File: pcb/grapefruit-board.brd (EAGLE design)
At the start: 100 x 50 mm, 151 parts, among them IC1 L70, IC10 TS520525, IC2 STC3100, IC3 TPS61200, IC4 LM3671MF, IC5 MCP73837MF, IC6 LM2840/1/2, IC7 STM32F411XC, IC8 S25FL064K, IC9 TLV320AIC3100, M1 ELECTRET_MICROPHON-WM-62PC/62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, Q1 BSS84, Q2 BSS84, Q3 BSS84, Q4 BSS84, X1 BU-SMA-V, X2 BU-SMA-V, X3 BU-SMA-V, X4 USB-MICROB, X5 USB-MICROB, Y1 32768Hz

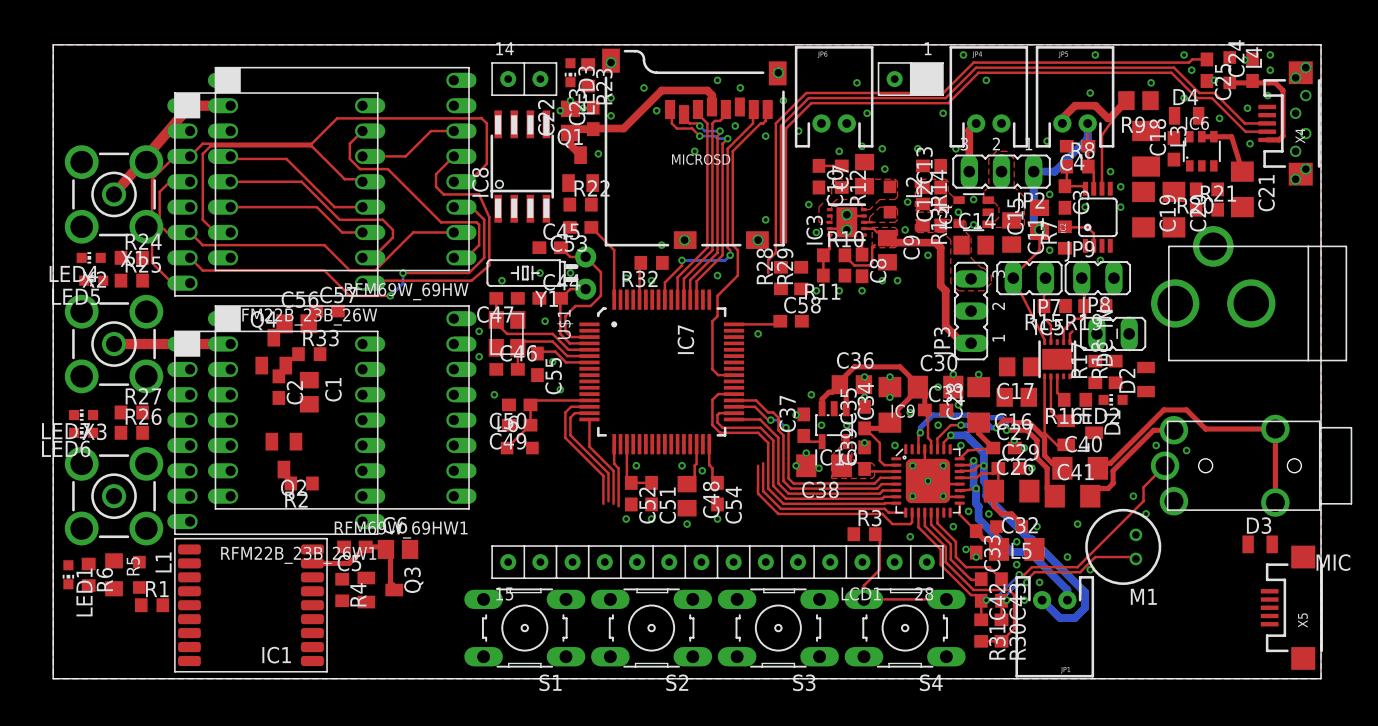
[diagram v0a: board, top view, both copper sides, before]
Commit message: Change values of some components, add SWD pin header
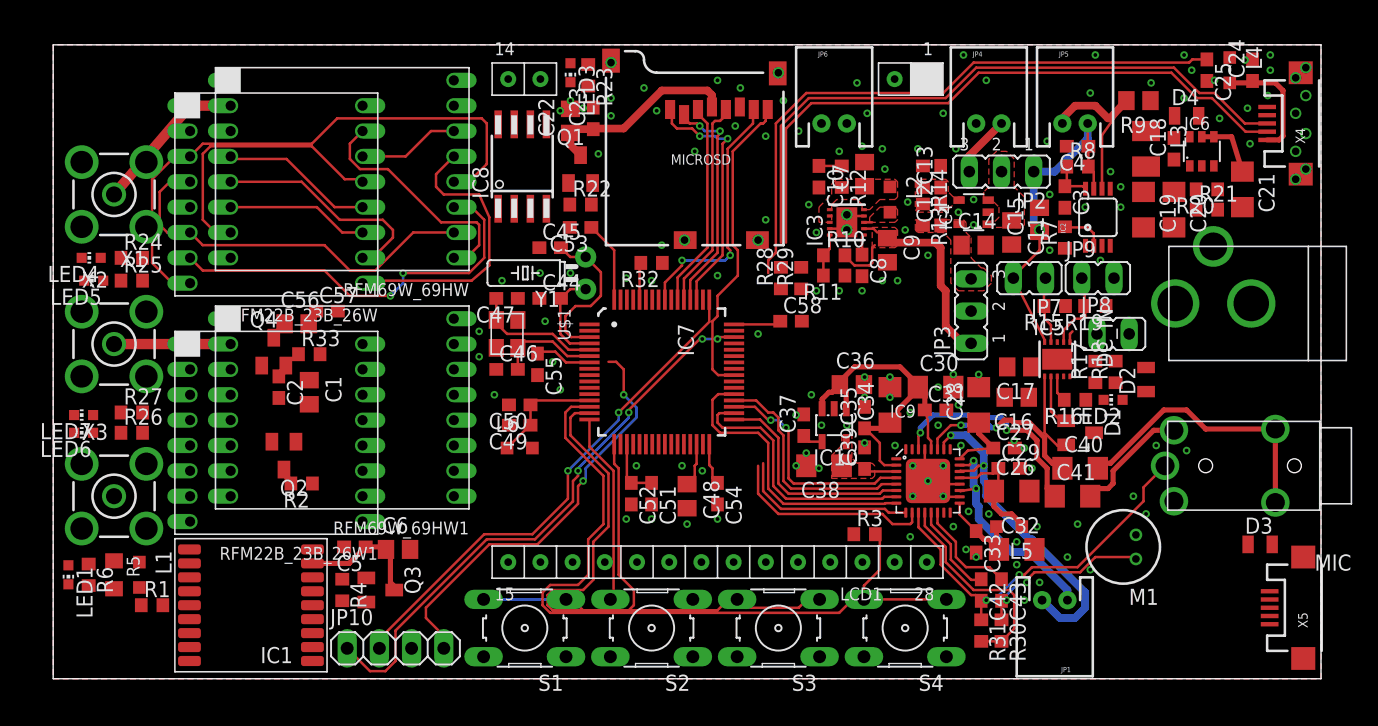
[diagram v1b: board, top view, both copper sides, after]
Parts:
- added JP10: (no value), pinhead:1X04
- C46, C47: value 12pF -> 22pF
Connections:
- removed net N$53: C55.1, IC7.7
- new net NRST: C55.1, IC7.7, JP10.4
- new net SWCLK: IC7.49, JP10.2
- new net SWDIO: IC7.46, JP10.1
- new net USART1_RX: IC7.55
- new net USART1_TX: IC7.50
- net GND: now also JP10.3, JP4.1; no longer JP4.2
- net N$10: now also JP4.2; no longer JP4.1
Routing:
- net SWDIO: track 0.00 -> 45.2 mm, vias 0 -> 4
- net SWCLK: track 0.00 -> 40.5 mm, vias 0 -> 2
- net NRST: track 0.00 -> 38.1 mm, vias 0 -> 2
- net BTN4: track 22.8 -> 60.1 mm
- net BTN3: track 9.49 -> 43.6 mm
- net BTN1: track 5.04 -> 25.7 mm
- net BTN2: track 7.44 -> 15.1 mm
- net N$53: track 4.51 -> 0.00 mm
- net N$10: track 4.02 -> 4.85 mm

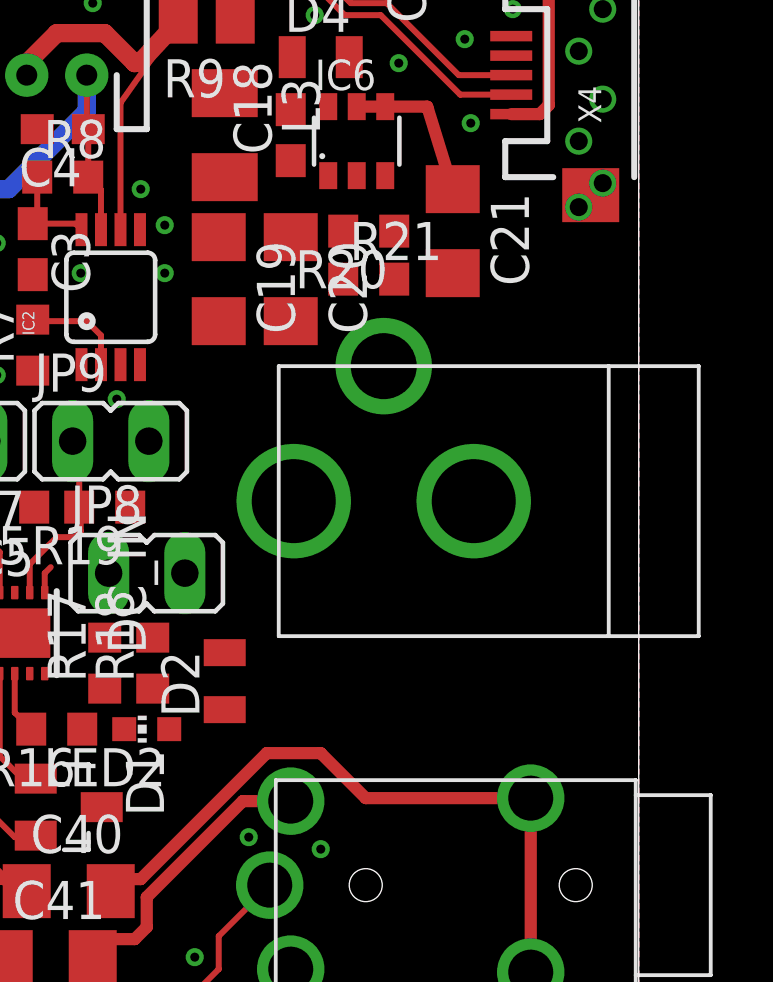
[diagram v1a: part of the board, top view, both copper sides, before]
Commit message: Add DC IN input
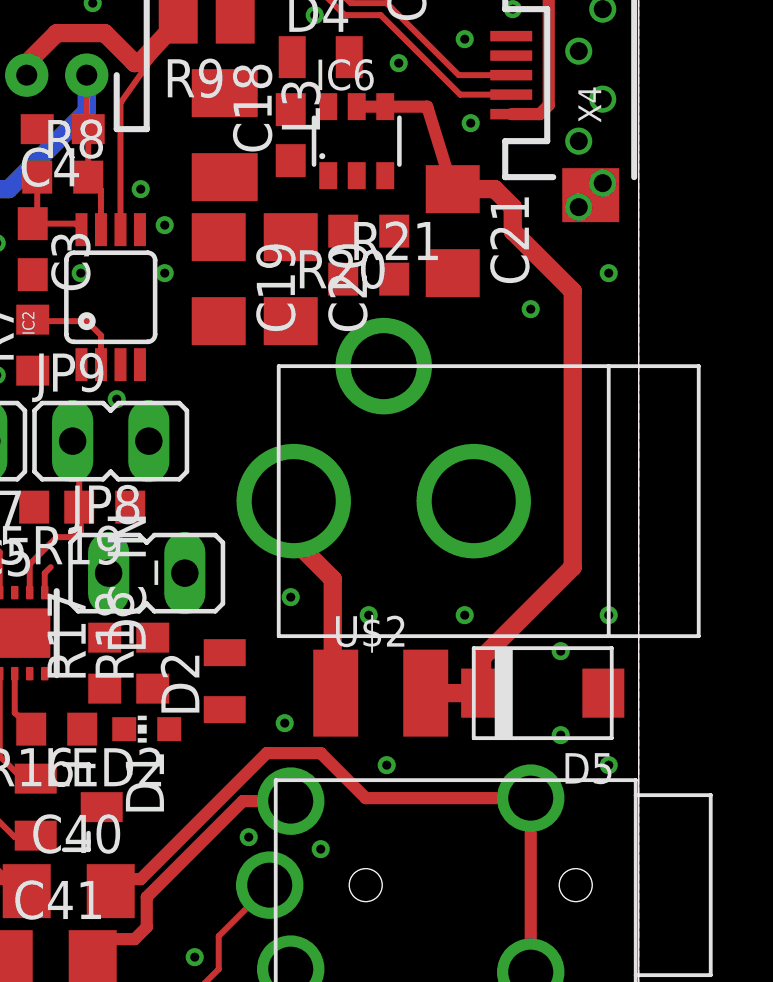
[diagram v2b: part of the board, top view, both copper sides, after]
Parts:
- added D5: 40V, qyx-misc:SMA_DIODE
- added U$2: PTC_FUSE1210, qyx-misc:PTC1210
- DC_IN: value DC_JACK -> 5-40V
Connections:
- new net N$53: DC_IN.C, U$2.1
- net DC_IN: now also D5.K, U$2.2
- net GND: now also D5.A, DC_IN.O, DC_IN.OSW
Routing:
- net DC_IN: track 5.23 -> 27.6 mm
- net N$53: track 0.00 -> 6.98 mm
- net GND: vias 143 -> 154
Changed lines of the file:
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@@
 <element name="MICROSD" library="SparkFun" package="MICRO-SD-SOCKET-PP" value="USD-SOCKETNEW" x="57.6" y="34.2"/>
 <element name="MIC" library="qyx-misc" package="JACK_35_4POLE" value="MJ-2135" x="102.4" y="16.8" rot="R180"/>
-<element name="DC_IN" library="con-qyx" package="DC_JACK" value="DC_JACK" x="95" y="29.6" rot="R90"/>
+<element name="DC_IN" library="con-qyx" package="DC_JACK" value="5-40V" x="95" y="29.6" rot="R90"/>
 <element name="M1" library="microphon" package="WM-62PC/62PK" value="ELECTRET_MICROPHON-WM-62PC/62PK" x="84.4" y="10.4" rot="R180">
 <attribute name="PN" value="PMOF-6027PN-42UQ" x="84.4" y="10.4" size="1.778" layer="27" rot="R180" display="off"/>
@@
 <element name="C58" library="rcl" package="C0603" value="100nF" x="58.2" y="28.2"/>
 <element name="JP10" library="pinhead" package="1X04" value="" x="27" y="2.4"/>
+<element name="U$2" library="qyx-misc" package="PTC1210" value="PTC_FUSE1210" x="91.4" y="23.2"/>
+<element name="D5" library="qyx-misc" package="SMA_DIODE" value="40V" x="96.8" y="23.2" rot="R180"/>
 </elements>
 <signals>
@@
 <contactref element="JP4" pad="1"/>
 <contactref element="JP10" pad="3"/>
+<contactref element="DC_IN" pad="O"/>
+<contactref element="DC_IN" pad="OSW"/>
+<contactref element="D5" pad="A"/>
+<via x="99" y="37.2" extent="1-16" drill="0.3"/>
+<via x="99" y="25.8" extent="1-16" drill="0.3"/>
+<via x="99" y="20.8" extent="1-16" drill="0.3"/>
+<via x="97.4" y="21.8" extent="1-16" drill="0.3"/>
+<via x="97.4" y="24.6" extent="1-16" drill="0.3"/>
+<via x="94.2" y="25.8" extent="1-16" drill="0.3"/>
+<via x="91" y="25.8" extent="1-16" drill="0.3"/>
+<via x="88.4" y="26.4" extent="1-16" drill="0.3"/>
+<via x="88.2" y="22.2" extent="1-16" drill="0.3"/>
+<via x="91.6" y="20.8" extent="1-16" drill="0.3"/>
+<via x="96.4" y="36" extent="1-16" drill="0.3"/>
 </signal>
 <signal name="N$3">
@@
 <wire x1="91.55" y1="42.75" x2="92.95" y2="42.75" width="0.4064" layer="1"/>
 <wire x1="92.95" y1="42.75" x2="93.8" y2="40" width="0.4064" layer="1"/>
+<contactref element="U$2" pad="2"/>
+<contactref element="D5" pad="K"/>
+<wire x1="92.9" y1="23.2" x2="94.78" y2="23.2" width="0.6096" layer="1"/>
+<wire x1="94.78" y1="23.2" x2="94.78" y2="24.38" width="0.6096" layer="1"/>
+<wire x1="94.78" y1="24.38" x2="97.8" y2="27.4" width="0.6096" layer="1"/>
+<wire x1="97.8" y1="27.4" x2="97.8" y2="36.6" width="0.6096" layer="1"/>
+<wire x1="97.8" y1="36.6" x2="95.8" y2="38.6" width="0.6096" layer="1"/>
+<wire x1="95.8" y1="38.6" x2="95.8" y2="39.4" width="0.6096" layer="1"/>
+<wire x1="95.8" y1="39.4" x2="95.2" y2="40" width="0.6096" layer="1"/>
+<wire x1="95.2" y1="40" x2="93.8" y2="40" width="0.6096" layer="1"/>
 </signal>
 <signal name="SDIO_D2">
@@
 <wire x1="25.73" y1="2.4" x2="25.73" y2="3.13" width="0.2" layer="1"/>
 </signal>
+<signal name="N$53">
+<contactref element="DC_IN" pad="C"/>
+<contactref element="U$2" pad="1"/>
+<wire x1="88.5" y1="29.6" x2="88.5" y2="28.3" width="0.6096" layer="1"/>
+<wire x1="88.5" y1="28.3" x2="89.8" y2="27" width="0.6096" layer="1"/>
+<wire x1="89.8" y1="27" x2="89.8" y2="23.3" width="0.6096" layer="1"/>
+<wire x1="89.8" y1="23.3" x2="89.9" y2="23.2" width="0.6096" layer="1"/>
+</signal>
 </signals>

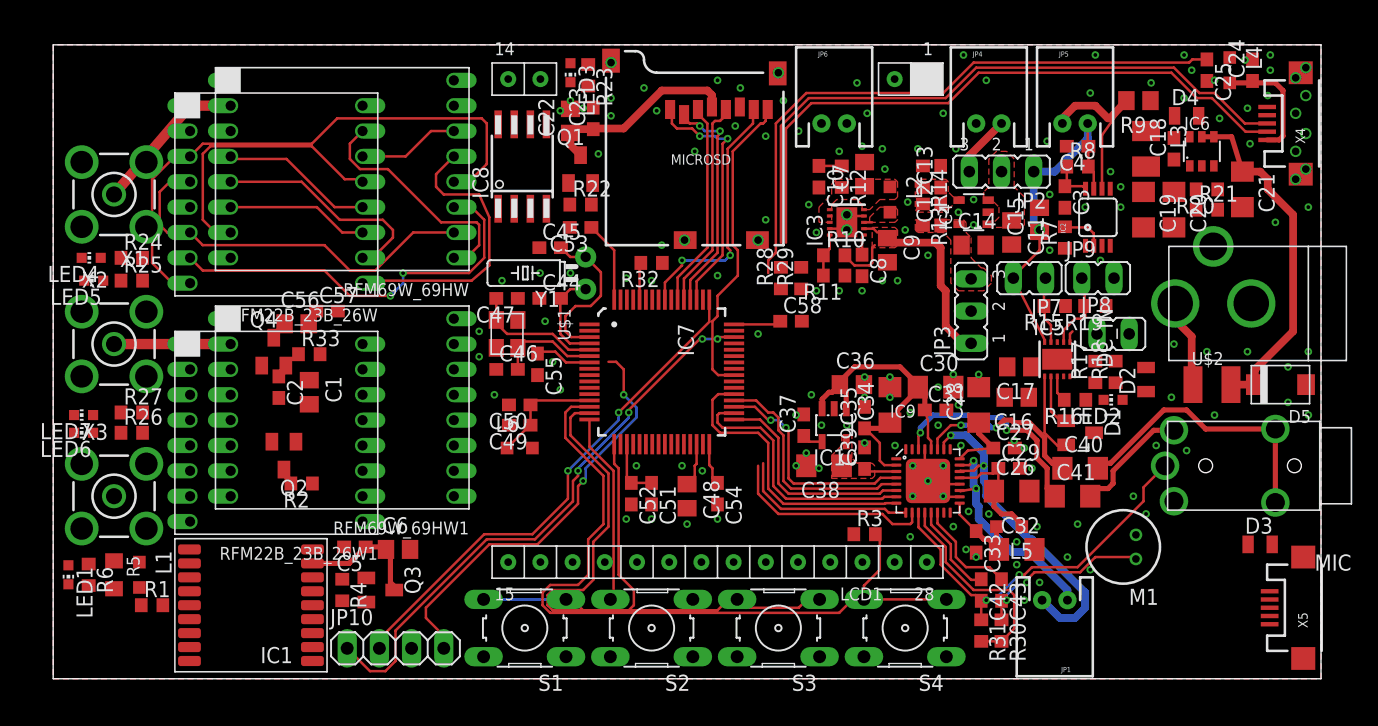
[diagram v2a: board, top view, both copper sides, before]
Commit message: Resolve the remaining unconnected parts
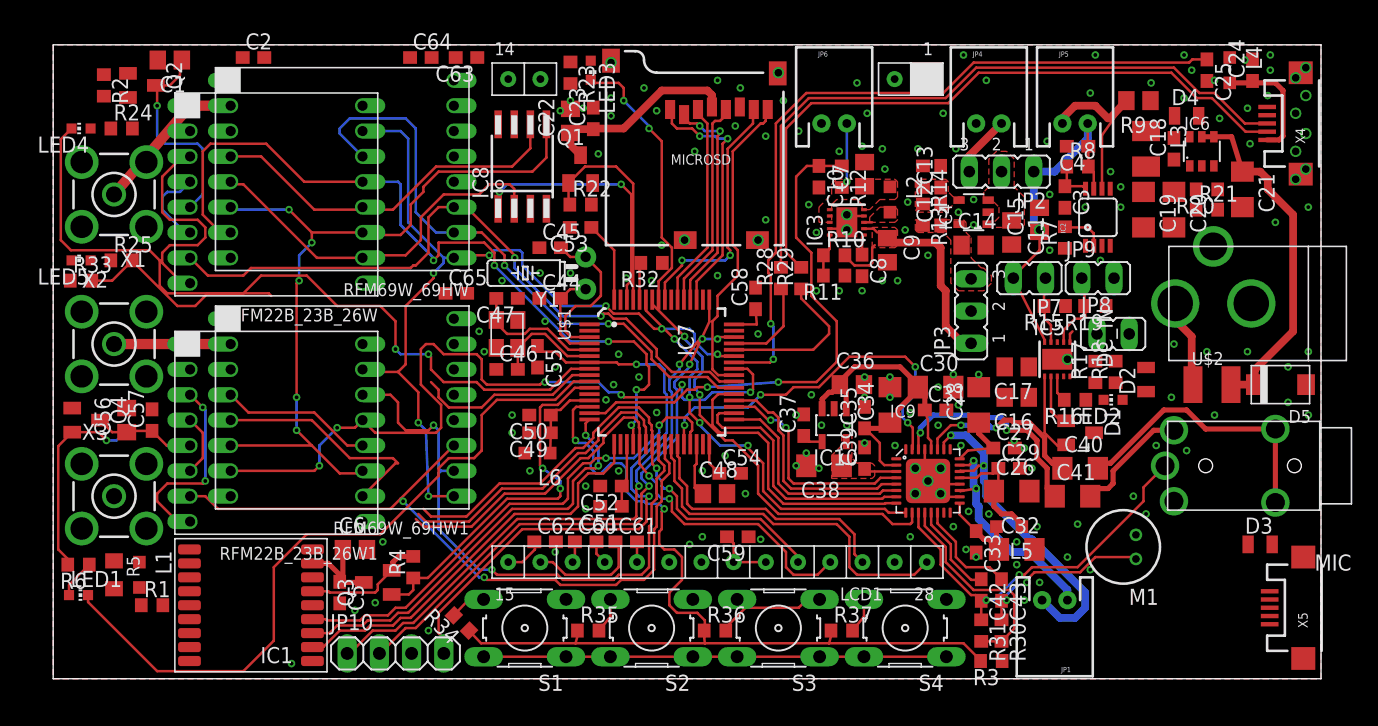
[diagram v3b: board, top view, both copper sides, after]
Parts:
- removed LED6, LED7: (no value), led:CHIP-LED0603
- removed R26, R27: 1K, rcl:R0603
- added C59, C63, C64, C65: 100nF, rcl:C0603
- added C60, C61, C62: 1uF, rcl:C0603
- added R34: 100K, rcl:R0603
- added R35: 47K, rcl:R0603
- added R36: 27K, rcl:R0603
- added R37: 10K, rcl:R0603
- R5: value VARISTORCN0805 -> (none)
- moved R2 35.1 mm to (4.00, 46.8), turned to 270 degrees
- moved Q2 31.3 mm to (7.00, 46.8), turned to 270 degrees
- moved C1 28.4 mm to (9.20, 48.8), turned to 180 degrees
- moved C2 26.1 mm to (15.8, 49.0), turned to 0 degrees
- moved R33 18.9 mm to (2.20, 31.4)
- moved C57 16.3 mm to (7.80, 20.4), turned to 90 degrees
- moved Q4 15.8 mm to (2.60, 20.4), turned to 270 degrees
- moved C56 15.4 mm to (5.80, 20.4), turned to 90 degrees
- moved R3 14.1 mm to (74.0, 1.40), turned to 180 degrees
- moved LED4 10.2 mm to (2.20, 43.4)
- moved R24 10.2 mm to (5.40, 43.4)
- moved R4 5.88 mm to (28.4, 8.80), turned to 90 degrees
- moved C5 3.79 mm to (22.6, 6.80), turned to 270 degrees
- moved C6 3.40 mm to (23.8, 10.2)
- moved C51 3.35 mm to (44.0, 13.6), turned to 180 degrees
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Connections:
- removed net CHG_FULL: IC5.4
- removed net CHG_PG: IC5.8
- removed net CODEC_RESET: IC9.31
- removed net N$33: LED6.A, R26.1
- removed net N$34: LED7.A, R27.1
- removed net R12_MISO: RFM22B_23B_26W.10, RFM22B_23B_26W1.10, RFM69W_69HW.5, RFM69W_69HW1.5
- removed net R12_MOSI: RFM22B_23B_26W.11, RFM22B_23B_26W1.11, RFM69W_69HW.6, RFM69W_69HW1.6
- removed net R12_SCK: RFM22B_23B_26W.12, RFM22B_23B_26W1.12, RFM69W_69HW.4, RFM69W_69HW1.4
- removed net R1_DIO1: RFM22B_23B_26W.7, RFM69W_69HW.11
- removed net R1_DIO3: RFM22B_23B_26W.9, RFM69W_69HW.13
- removed net R1_DIO4: RFM22B_23B_26W.14, RFM69W_69HW.14
- removed net R1_DIO5: RFM69W_69HW.15
- removed net R1_LED1: LED4.C
- removed net R1_LED2: LED5.C
- removed net R1_NSS: RFM22B_23B_26W.13, RFM69W_69HW.7
- removed net R1_RESET: RFM22B_23B_26W.15, RFM69W_69HW.9
- removed net R2_DIO1: RFM22B_23B_26W1.7, RFM69W_69HW1.11
- removed net R2_DIO3: RFM22B_23B_26W1.9, RFM69W_69HW1.13
- removed net R2_DIO4: RFM22B_23B_26W1.14, RFM69W_69HW1.14
- removed net R2_DIO5: RFM69W_69HW1.15
- removed net R2_LED1: LED6.C
- removed net R2_LED2: LED7.C
- removed net R2_NSS: RFM22B_23B_26W1.13, RFM69W_69HW1.7
- removed net R2_RESET: RFM22B_23B_26W1.15, RFM69W_69HW1.9
- removed net VCC: IC8.8
- new net BTN: IC7.14, R3.2, R34.1, R35.1, R36.1, R37.1
- new net CODEC_RST: IC7.28, IC9.31
- new net FLASH1_CS: IC7.62, IC8.1
- new net LCD_CD: IC7.27, LCD1.26
- new net LCD_CS: IC7.26, LCD1.28
- new net N$60: C60.1, LCD1.17
- new net N$61: C61.1, LCD1.16
- new net N$62: C60.2, LCD1.18
- new net N$63: C61.2, LCD1.19
- new net N$64: C62.1, LCD1.15
- new net R12_RESET: IC7.43, RFM22B_23B_26W.15, RFM22B_23B_26W1.15, RFM69W_69HW.9, RFM69W_69HW1.9
- new net R1_CS: IC7.20, RFM22B_23B_26W.13, RFM69W_69HW.7
- new net R1_IRQ0: IC7.38, RFM22B_23B_26W.14, RFM69W_69HW.10
- new net R1_IRQ1: IC7.39, RFM22B_23B_26W.7, RFM69W_69HW.11
- new net R1_LED: IC7.8, LED4.C
- new net R2_CS: IC7.41, RFM22B_23B_26W1.13, RFM69W_69HW1.7
- new net R2_IRQ0: IC7.24, RFM22B_23B_26W1.14, RFM69W_69HW1.10
- new net R2_IRQ1: IC7.25, RFM22B_23B_26W1.7, RFM69W_69HW1.11
- new net R2_LED: IC7.9, LED5.C
- new net SPI1_MISO: IC7.22, IC8.2, RFM22B_23B_26W.10, RFM22B_23B_26W1.10, RFM69W_69HW.5, RFM69W_69HW1.5
- new net SPI1_MOSI: IC7.23, IC8.5, LCD1.24, RFM22B_23B_26W.11, RFM22B_23B_26W1.11, RFM69W_69HW.6, RFM69W_69HW1.6
- new net SPI1_SCK: IC7.21, IC8.6, LCD1.25, RFM22B_23B_26W.12, RFM22B_23B_26W1.12, RFM69W_69HW.4, RFM69W_69HW1.4
- net +3V3: now also C59.2, C63.1, IC8.8, LCD1.22, LCD1.23; no longer R26.2, R27.2, RFM69W_69HW.16, RFM69W_69HW1.16
- net BTN1: now also R34.2; no longer IC7.17, S1.3
- net BTN2: now also R35.2; no longer IC7.16, S2.3
- net BTN3: now also R36.2; no longer IC7.15, S3.3
- net BTN4: now also R37.2; no longer IC7.14, R3.2, S4.3
- net CHG_CHG: now also IC2.1
- net GND: now also C59.1, C62.2, C63.2, C64.2, C65.2, LCD1.20, LCD1.21
- net GPS_LED: now also IC7.10
- net GPS_PPS: now also IC7.29
- net GPS_PWR: now also IC7.11
- net N$56: now also C65.1, RFM69W_69HW1.16
- net N$6: now also C64.1, RFM69W_69HW.16
- net R1_DIO0: no longer RFM69W_69HW.10
- net R1_DIO2: no longer RFM69W_69HW.12
- net R2_DIO0: no longer RFM69W_69HW1.10
- net R2_DIO2: no longer RFM69W_69HW1.12
- net SCL: now also IC7.58
- net SDA: now also IC7.59
- net SD_LED: now also IC7.57
- net SD_PWR: now also IC7.61
- net USART2_RX: now also IC7.17
- net USART2_TX: now also IC7.16
- net VBAT15_U: now also IC7.15
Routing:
- net SPI1_MOSI: track 0.00 -> 103.4 mm, vias 0 -> 7
- net SPI1_SCK: track 0.00 -> 87.4 mm, vias 0 -> 2
- net +3V3: track 61.3 -> 144.6 mm, vias 0 -> 1
- net BTN: track 0.00 -> 73.9 mm, vias 0 -> 2
- net SPI1_MISO: track 0.00 -> 72.6 mm
- net R12_RESET: track 0.00 -> 68.0 mm, vias 0 -> 7
- net R1_CS: track 0.00 -> 62.4 mm, vias 0 -> 5
- net R2_CS: track 0.00 -> 60.6 mm, vias 0 -> 6
- net R1_LED: track 0.00 -> 60.6 mm, vias 0 -> 2
- net BTN4: track 60.1 -> 2.78 mm
- net GPS_LED: track 0.00 -> 57.2 mm
- net R2_IRQ1: track 0.00 -> 57.1 mm, vias 0 -> 2
- net R1_IRQ1: track 0.00 -> 54.2 mm, vias 0 -> 2
- net R1_IRQ0: track 0.00 -> 47.9 mm, vias 0 -> 2
- net R2_IRQ0: track 0.00 -> 46.4 mm, vias 0 -> 2
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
